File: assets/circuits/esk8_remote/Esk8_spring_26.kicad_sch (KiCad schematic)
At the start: 56 parts

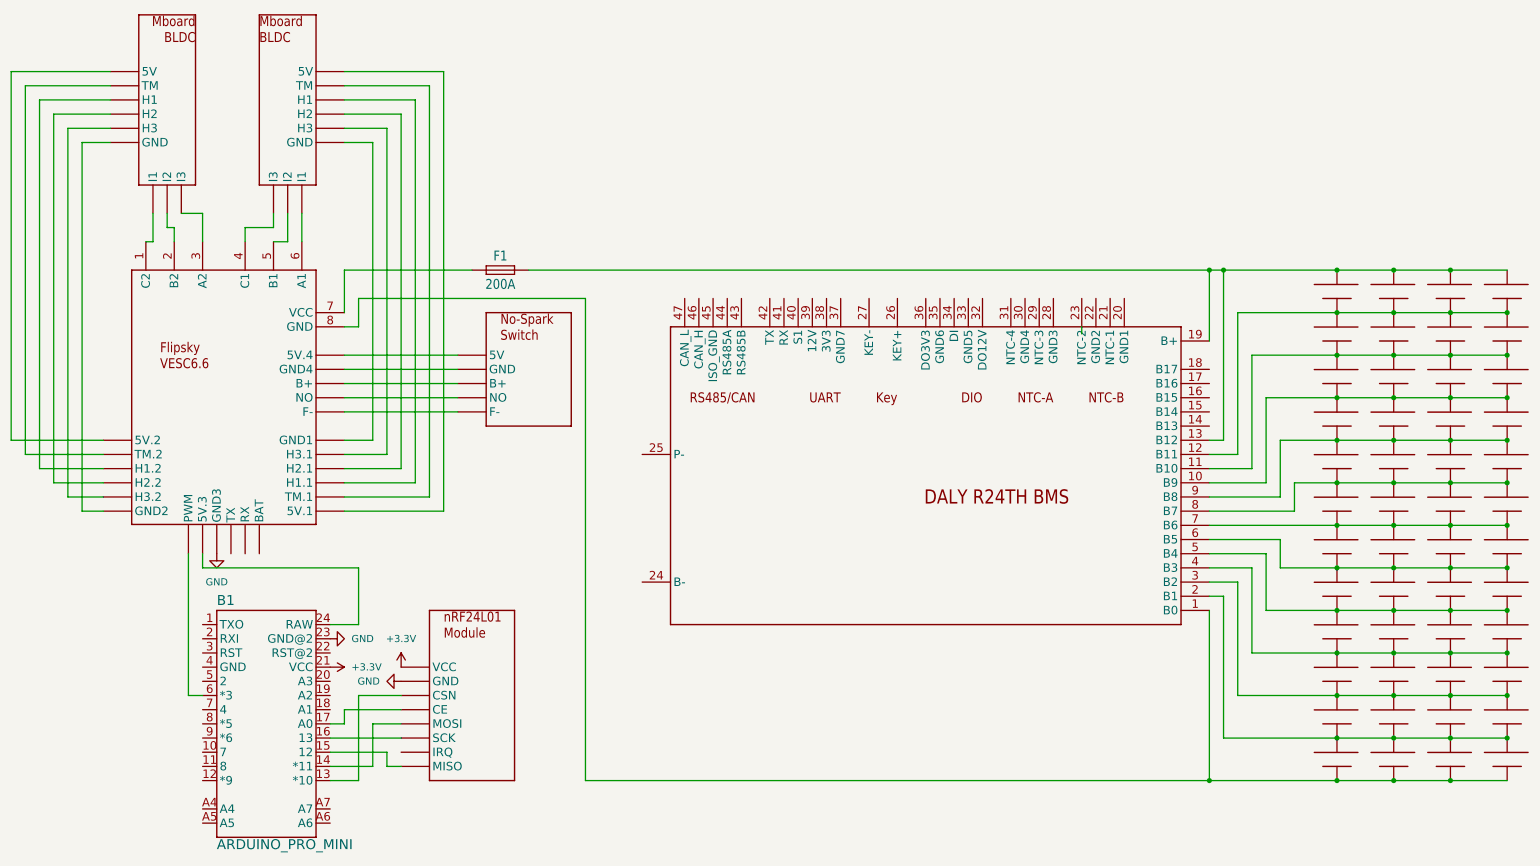
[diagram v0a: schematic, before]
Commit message: delete incorrect base schematic
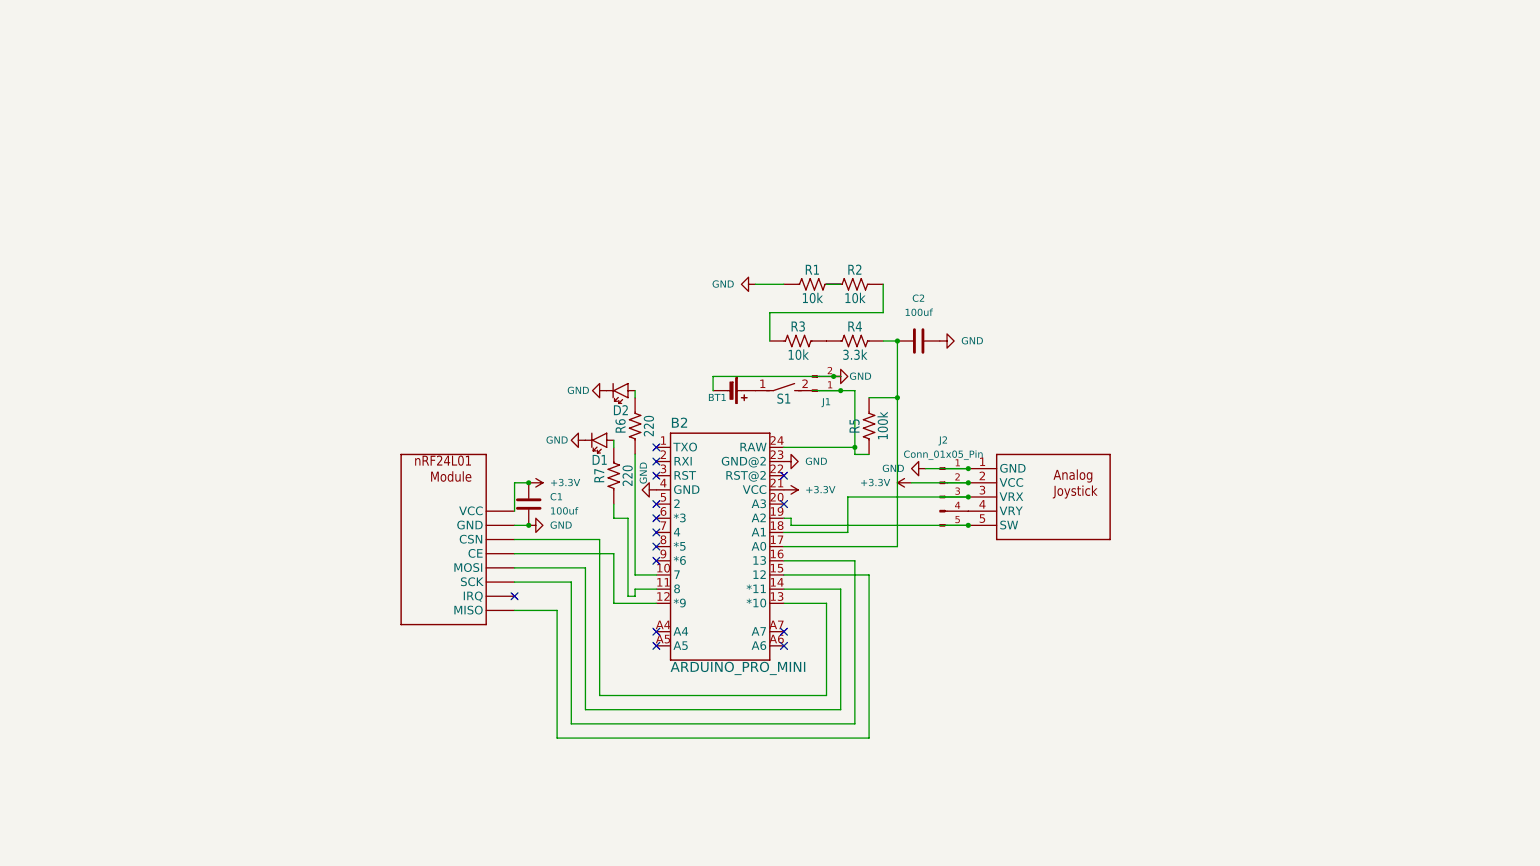
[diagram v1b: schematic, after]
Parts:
- removed #U$1: FLIPSKYVESC, symbol Esk8_spring_26-eagle-import:FLIPSKYVESC
- removed #U$10, #U$11, #U$12, #U$13, #U$14, #U$15, #U$16, #U$17, #U$18, #U$19, #U$20, #U$21, #U$22, #U$23, #U$24, #U$25, #U$26, #U$27, #U$28, #U$29, #U$30, #U$31, #U$32, #U$33, #U$34, #U$35, #U$36, #U$37, #U$38, #U$39, #U$40, #U$41, #U$42, #U$43, #U$44, #U$45, #U$46, #U$47, #U$48, #U$49, #U$50, #U$51, #U$52, #U$53, #U$54, #U$55, #U$56, #U$57: 21700, symbol Esk8_spring_26-eagle-import:21700
- removed #U$2, #U$3: MBOARDMOTOR, symbol Esk8_spring_26-eagle-import:MBOARDMOTOR
- removed #U$4: NRF-MODULE, symbol Esk8_spring_26-eagle-import:NRF-MODULE
- removed #U$5: NO-SPARK-SWITCH, symbol Esk8_spring_26-eagle-import:NO-SPARK-SWITCH
- removed #U$9: DALY_R24TH, symbol Esk8_spring_26-eagle-import:DALY_R24TH
- removed B1: ARDUINO_PRO_MINI, ArduinoProMini:ProMini, symbol Esk8_spring_26-eagle-import:ARDUINO_PRO_MINI
- removed F1: 200A, symbol Esk8_spring_26-eagle-import:1812L
- added #U$6: ANALOG_JOYSITCK, symbol Esk8_spring_26-eagle-import:ANALOG_JOYSITCK
- added B2: ARDUINO_PRO_MINI, ArduinoProMini:ProMini, symbol Esk8_spring_26-eagle-import:ARDUINO_PRO_MINI
- added BT1: Battery_Cell, symbol Device:Battery_Cell
- added C1, C2: 100uf, Capacitor_THT:C_Disc_D5.0mm_W2.5mm_P5.00mm, symbol Device:C
- added D1, D2: CHIP-FLAT-B_0603-0.35MM, LED_THT:LED_D5.0mm, symbol Esk8_spring_26-eagle-import:CHIP-FLAT-B_0603-0.35MM
- added J1: Conn_01x02_Pin, Connector:JWT_A3963_1x02_P3.96mm_Vertical, symbol Connector:Conn_01x02_Pin
- added J2: Conn_01x05_Pin, Connector_PinHeader_2.54mm:PinHeader_1x05_P2.54mm_Vertical, symbol Connector:Conn_01x05_Pin
- added R1, R2, R3: 10k, Resistor_THT:R_Axial_DIN0207_L6.3mm_D2.5mm_P10.16mm_Horizontal, symbol Esk8_spring_26-eagle-import:R-USCHIP-0402(1005-METRIC)
- added R4: 3.3k, Resistor_THT:R_Axial_DIN0207_L6.3mm_D2.5mm_P10.16mm_Horizontal, symbol Esk8_spring_26-eagle-import:R-USCHIP-0402(1005-METRIC)
- added R5: 100k, Resistor_THT:R_Axial_DIN0207_L6.3mm_D2.5mm_P10.16mm_Horizontal, symbol Esk8_spring_26-eagle-import:R-USCHIP-0402(1005-METRIC)
- added R6, R7: 220, Resistor_THT:R_Axial_DIN0207_L6.3mm_D2.5mm_P10.16mm_Horizontal, symbol Esk8_spring_26-eagle-import:R-USCHIP-0402(1005-METRIC)
- added S1: DS01E, symbol Esk8_spring_26-eagle-import:DS01E
- added U8: NRF-MODULE, symbol Esk8_spring_26-eagle-import:NRF-MODULE
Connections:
- net +3.3V: now also #U$6.2 (VCC), B2.21 (VCC), C1.1, J2.2 (Pin_2), U8.2 (VCC)
- net GND: now also #U$6.1 (GND), B2.23 (GND@2), B2.4 (GND), BT1.2 (-), C1.2, C2.2, D1.2 (C), D2.2 (C), J1.2 (Pin_2), J2.1 (Pin_1), R1.1, U8.1 (GND)
- new net: R3.2, R4.1
- new net: B2.17 (A0), C2.1, R4.2, R5.2
- new net: BT1.1 (+), S1.1
- new net: #U$6.3 (VRX), B2.18 (A1), J2.3 (Pin_3)
- new net: #U$6.4 (VRY), J2.4 (Pin_4)
- new net: #U$6.5 (SW), B2.19 (A2), J2.5 (Pin_5)
- new net: B2.24 (RAW), J1.1 (Pin_1), R5.1, S1.2
- new net: B2.10 (7), R6.1
- new net: D2.1 (A), R6.2
- new net: B2.11 (8), R7.1
- new net: D1.1 (A), R7.2
- new net: R1.2, R2.1
- new net: B2.12 (*9), U8.3 (CE)
- new net: B2.13 (*10), U8.4 (CSN)
- new net: B2.16 (13), U8.5 (SCK)
- new net: B2.14 (*11), U8.6 (MOSI)
- new net: B2.15 (12), U8.7 (MISO)
- new net: R2.2, R3.1
- no-connect marks 0 -> 15

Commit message: bro I spent 3 hours and changed nothing😭
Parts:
- removed U8: NRF-MODULE, symbol Esk8_spring_26-eagle-import:NRF-MODULE
- added U1: NRF24L01_Breakout, RF_Module:nRF24L01_Breakout, symbol RF:NRF24L01_Breakout
- #U$6: symbol Esk8_spring_26-eagle-import:ANALOG_JOYSITCK -> Esk8 symbols:ANALOG_JOYSITCK
- B2: symbol Esk8_spring_26-eagle-import:ARDUINO_PRO_MINI -> Esk8 symbols:ARDUINO_PRO_MINI
- C1, C2: value 100uf -> 100nf
- D1, D2: symbol Esk8_spring_26-eagle-import:CHIP-FLAT-B_0603-0.35MM -> Device:LED
- J1: footprint Connector:JWT_A3963_1x02_P3.96mm_Vertical -> Connector_PinHeader_2.54mm:PinHeader_1x02_P2.54mm_Vertical
- R1, R2, R3, R4, R5, R6, R7: symbol Esk8_spring_26-eagle-import:R-USCHIP-0402(1005-METRIC) -> Device:R_US
- S1: symbol Esk8_spring_26-eagle-import:DS01E -> Switch:SW_SPST
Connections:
- net +3.3V: now also U1.2 (VCC)
- net GND: now also D1.1 (K), D2.1 (K), R1.2, U1.1 (GND); no longer D1.2 (C), D2.2 (C), R1.1
- net at R3.2: now also R2.1; no longer R4.1
- net VDIV: now reaches B2.17 (A0), C2.1
- net VDIV: now also R4.1, R5.1; no longer R4.2, R5.2
- net VRX: now reaches #U$6.3 (VRX), B2.18 (A1), J2.3 (Pin_3)
- net SW: now reaches #U$6.5 (SW), B2.19 (A2), J2.5 (Pin_5)
- net at B2.24 (RAW), J1.1 (Pin_1), S1.2 (B): now also R5.2; no longer R5.1
- net at R6.2: now also D2.2 (A); no longer D2.1 (A)
- net at R7.2: now also D1.2 (A); no longer D1.1 (A)
- net CE: now reaches B2.12 (*9)
- net CE: now also U1.3 (CE)
- net CSN: now reaches B2.13 (*10)
- net CSN: now also U1.4 (~{CSN})
- net SCK: now reaches B2.16 (13)
- net SCK: now also U1.5 (SCK)
- net MOSI: now reaches B2.14 (*11)
- net MOSI: now also U1.6 (MOSI)
- net MISO: now reaches B2.15 (12)
- net MISO: now also U1.7 (MISO)
- net at R3.1: now also R4.2; no longer R2.2
- new net: R1.1, R2.2
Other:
- moved on the sheet: C1
